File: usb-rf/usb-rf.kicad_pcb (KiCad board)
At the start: 4 copper layers, 46.7 x 18.3 mm, 45 parts, among them J1 USB_B_Micro, J2 SMA, J3 ARM 10 pin, U1 STM32L432KBUx, U2 XC6206PxxxMR, U3 USBLC6-2SC6, U4 nRF24L01P, Y1 16 MHz

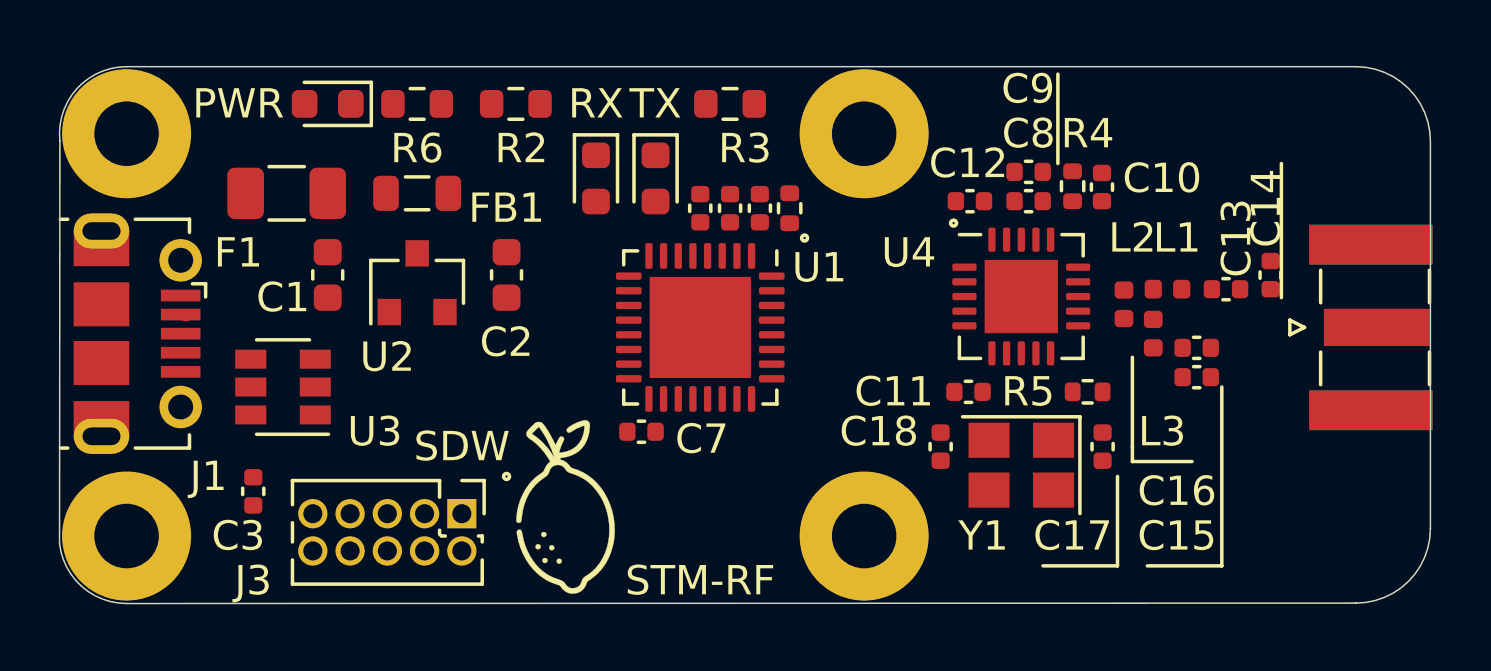
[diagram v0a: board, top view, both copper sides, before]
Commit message: stm-rf: include differential routing
Signed-off-by: SeanTedesco <stedesco@live.com>
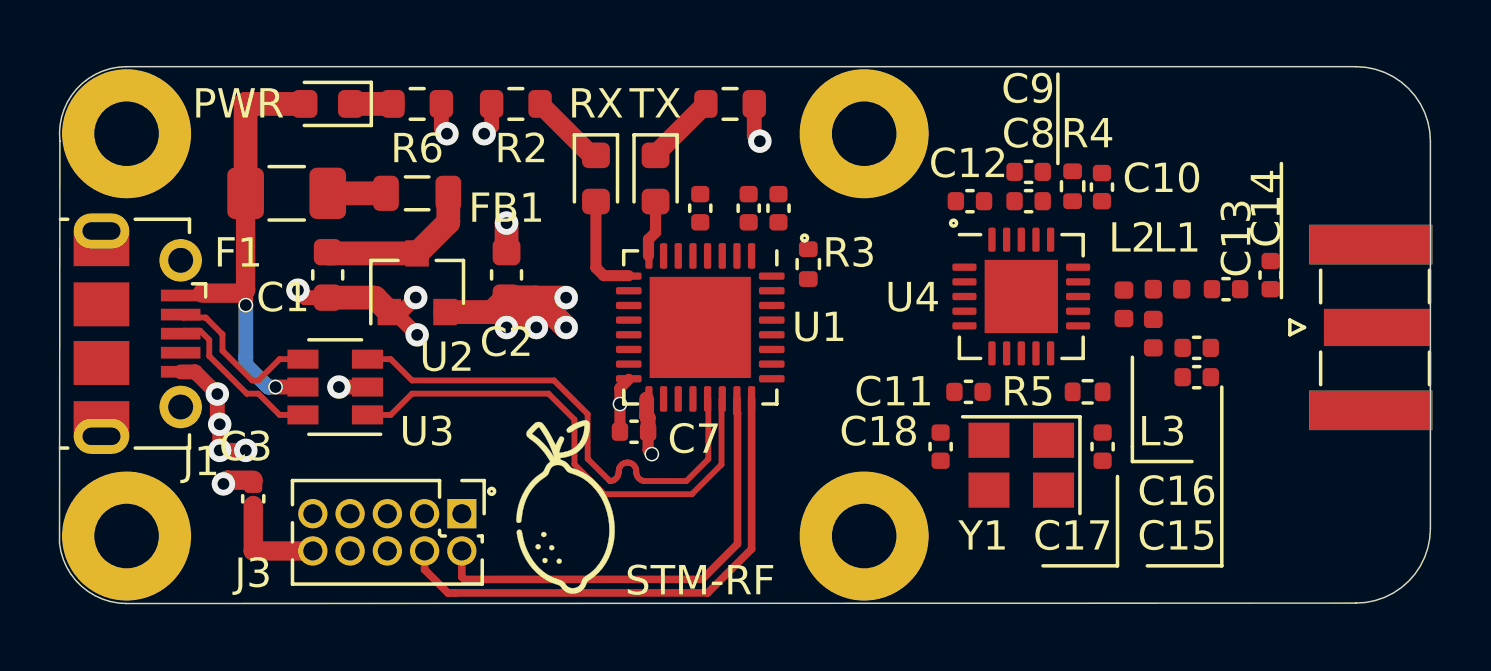
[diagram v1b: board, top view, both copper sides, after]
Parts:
- moved R1 2.01 mm to (141.9, 79.6)
- moved U3 1.78 mm to (125.7, 83.8)
- moved C4 0.63 mm to (140.8, 77.7)
- moved C5 0.63 mm to (139.8, 77.7)
- moved C3 0.25 mm to (122.9, 87.6)
- moved C7 0.25 mm to (135.9, 85.3)
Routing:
- net GND: track 0.00 -> 18.7 mm, vias 0 -> 14
- net SWCLK: track 0.00 -> 17.8 mm
- net USB_D-: track 0.00 -> 17.4 mm
- net USB_D+: track 0.00 -> 17.3 mm
- net SWDIO: track 0.00 -> 15.8 mm
- net +5V: track 0.00 -> 14.7 mm, vias 0 -> 2
- net +3V3: track 0.00 -> 11.2 mm, vias 0 -> 5
- net USB_CONN_D+: track 0.00 -> 5.72 mm
- net USB_CONN_D-: track 0.20 -> 5.86 mm
- net Net-(C1-Pad1): track 0.00 -> 5.55 mm
- net NRST: track 0.00 -> 3.58 mm
- net Net-(D1-Pad2): track 0.00 -> 3.49 mm
- net Net-(D1-Pad1): track 0.00 -> 2.63 mm
- net Net-(D2-Pad1): track 0.00 -> 2.46 mm
- net Net-(F1-Pad2): track 0.00 -> 1.99 mm
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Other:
- board text removed: "SDW"

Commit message: stm-rf: add routing for spi connections
Signed-off-by: Sean Tedesco <stedesco@live.com>
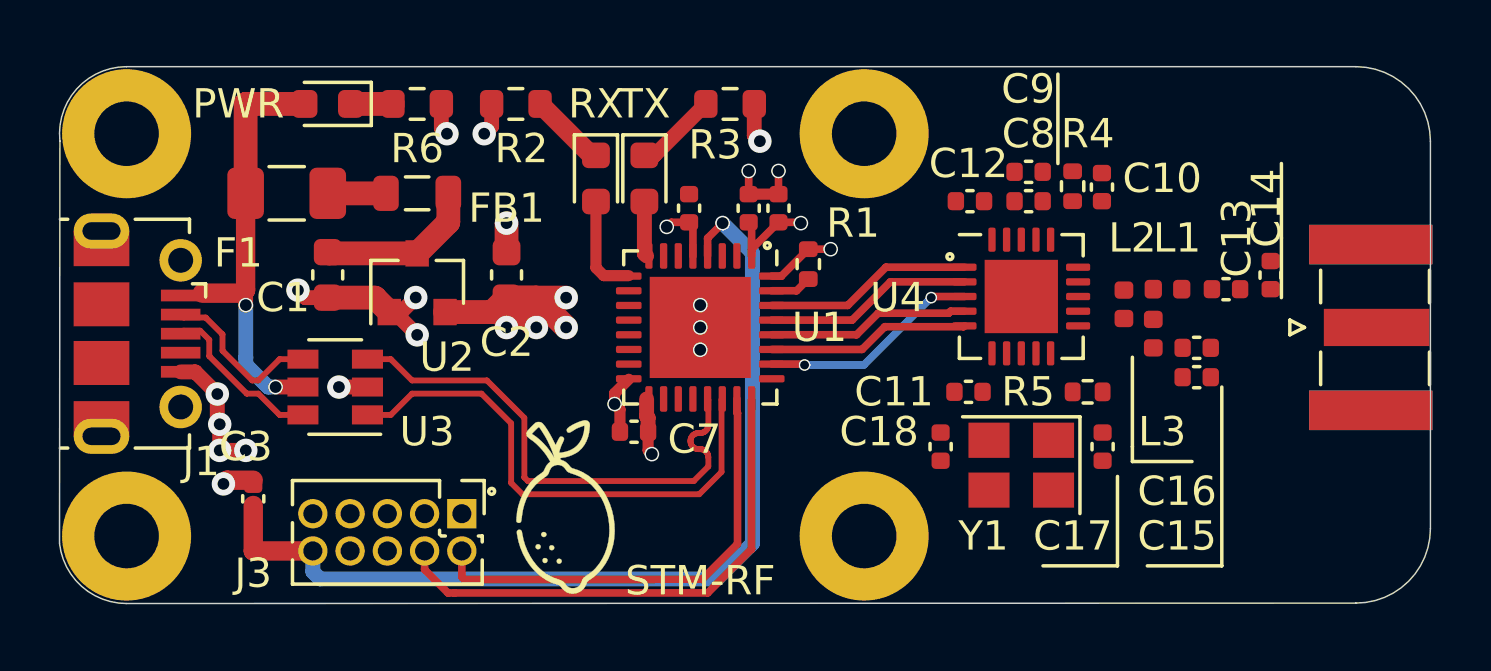
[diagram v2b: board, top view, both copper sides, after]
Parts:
- moved C6 0.38 mm to (137.8, 77.7)
- moved TX 0.38 mm to (136.3, 76.7)
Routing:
- net NRST: track 3.58 -> 32.6 mm, vias 0 -> 1
- net SPI3_SCK: track 0.00 -> 7.55 mm, vias 0 -> 2
- net SPI3_CSN: track 0.00 -> 7.11 mm
- net NRF_CE: track 0.00 -> 7.11 mm
- net SPI3_MOSI: track 0.00 -> 6.90 mm
- net SPI3_MISO: track 0.00 -> 6.90 mm
- net +3V3: track 11.2 -> 16.7 mm, vias 5 -> 7
- net GND: track 18.7 -> 23.9 mm, vias 14 -> 20
- net Net-(R1-Pad1): track 0.00 -> 1.41 mm

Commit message: stm-rf: add controlled impedance traces for RF
Signed-off-by: Sean Tedesco <stedesco@live.com>
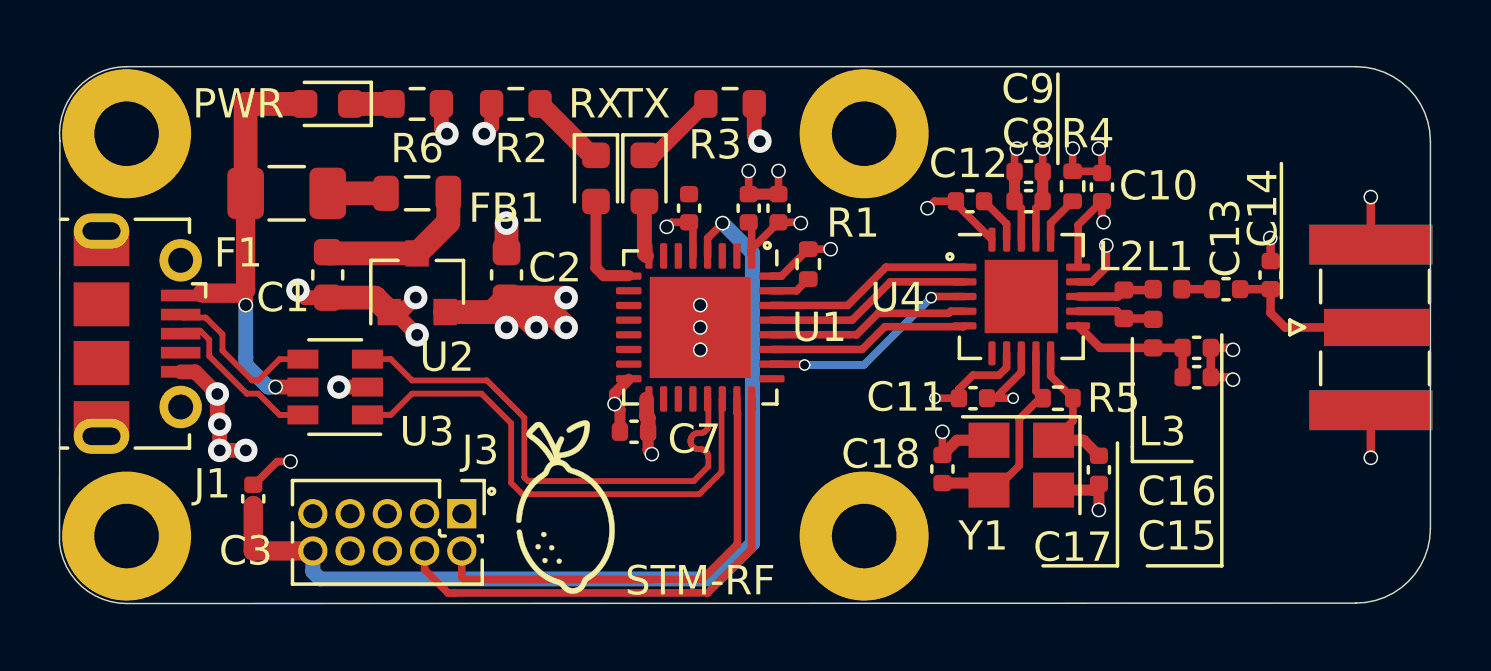
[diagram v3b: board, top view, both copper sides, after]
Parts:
- moved R5 1.04 mm to (150.4, 84.2)
- moved C17 0.80 mm to (151.8, 86.6)
- moved C18 0.76 mm to (146.4, 86.6)
- moved C11 0.27 mm to (147.5, 84.2), turned to 0 degrees
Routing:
- net GND: track 23.9 -> 51.7 mm, vias 20 -> 33
- net +3V3: track 16.7 -> 26.9 mm, vias 7 -> 10
- net NRF_XC2: track 0.00 -> 7.39 mm
- net Net-(C13-Pad1): track 0.00 -> 5.67 mm
- net NRF_XC1: track 0.00 -> 5.31 mm
- net NRF_VDD_PA: track 0.00 -> 4.87 mm
- net NRF_ANT1: track 0.00 -> 2.68 mm
- net NRF_ANT2: track 0.00 -> 2.67 mm
- net Net-(C12-Pad1): track 0.00 -> 1.63 mm
- net Net-(R4-Pad1): track 0.00 -> 1.62 mm
- net Net-(C13-Pad2): track 0.00 -> 1.03 mm

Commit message: usb-rf: continue with rf guard ring
Signed-off-by: SeanTedesco <stedesco@live.com>
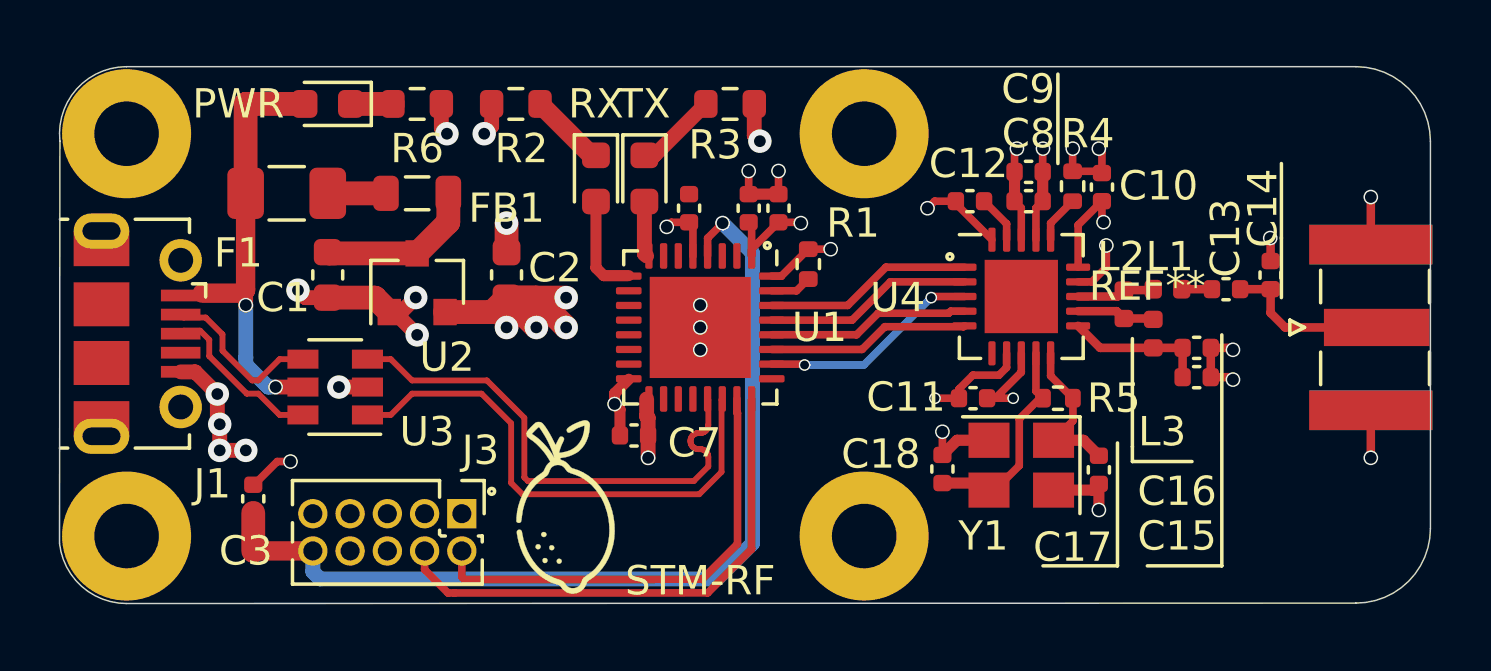
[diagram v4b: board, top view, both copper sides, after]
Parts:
- added REF**: stm-rf-guard-ring-1, usb-rf:stm-rf-guard-ring-1, F.Cu at (153.4, 79.9)
- moved C7 0.13 mm to (135.9, 85.5)

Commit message: usb-rf: include step and rf guard ring
just need manufacturing files!

Signed-off-by: Sean Tedesco <stedesco@live.com>
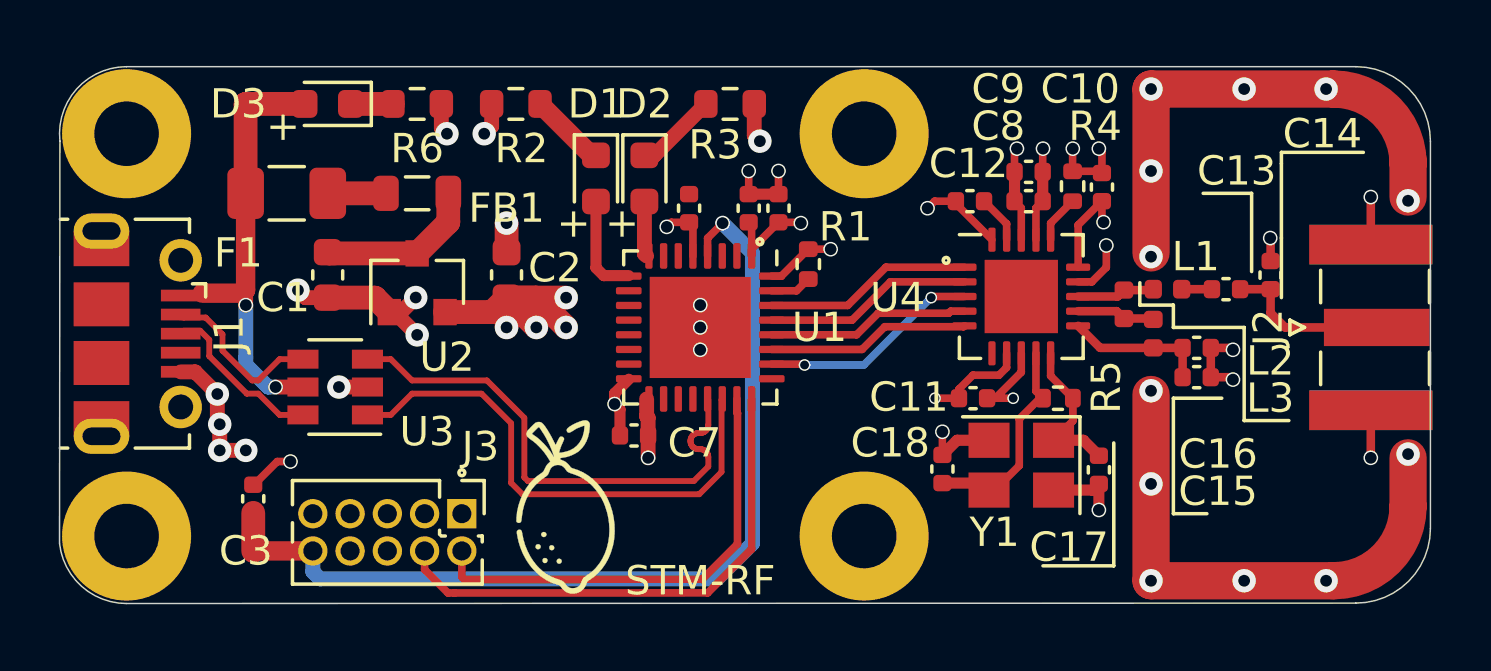
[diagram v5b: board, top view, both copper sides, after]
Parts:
- removed the REF** at (153.4, 79.9)
- added REF**: guard-ring-v1, footprints:guard-ring-v1, F.Cu at (153.7, 79.2)
- J1: footprint Connector_USB:USB_Micro-B_Molex-105017-0001 -> footprints:USB_Micro-B_Molex-105017-0001-SeanCopy
- J2: footprint Connector_Coaxial:SMA_Samtec_SMA-J-P-X-ST-EM1_EdgeMount -> footprints:SMA_Samtec_SMA-J-P-X-ST-EM1_EdgeMount-SeanCopyy
- renumbered RX to D1, TX to D2, PWR to D3
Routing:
- net GND: vias 33 -> 45
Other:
- board text added: "+"
